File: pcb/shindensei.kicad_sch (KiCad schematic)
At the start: 0 parts

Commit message: Switch matrix output
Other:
- added sheet Channel Switch Matrix (switch_matrix.kicad_sch)
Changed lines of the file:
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@@
     (comment 1 "${Project}")
+  )
+  (sheet (at 143.51 88.9) (size 33.02 29.21) (fields_autoplaced)
+    (stroke (width 0.1524) (type solid))
+    (fill (color 0 0 0 0.0000))
+    (property "Sheetname" "Channel Switch Matrix" (at 143.51 88.1884 0)
+      (effects (font (size 1.27 1.27)) (justify left bottom))
+    )
+    (property "Sheetfile" "switch_matrix.kicad_sch" (at 143.51 118.6946 0)
+      (effects (font (size 1.27 1.27)) (justify left top))
+    )
+    (pin "CH1_B" output (at 176.53 96.52 0)
+      (effects (font (size 1.27 1.27)) (justify right))
+    )
+    (pin "PLS_A" input (at 163.83 88.9 90)
+      (effects (font (size 1.27 1.27)) (justify right))
+    )
+    (pin "PLS_B" input (at 154.94 88.9 90)
+      (effects (font (size 1.27 1.27)) (justify right))
+    )
+    (pin "CH1_A" output (at 176.53 93.98 0)
+      (effects (font (size 1.27 1.27)) (justify right))
+    )
+    (pin "CH2_B" output (at 176.53 111.76 0)
+      (effects (font (size 1.27 1.27)) (justify right))
+    )
+    (pin "CH2_A" output (at 176.53 109.22 0)
+      (effects (font (size 1.27 1.27)) (justify right))
+    )
+    (pin "OUT_A0" input (at 143.51 100.33 180)
+      (effects (font (size 1.27 1.27)) (justify left))
+    )
+    (pin "OUT_A1" input (at 143.51 106.68 180)
+      (effects (font (size 1.27 1.27)) (justify left))
+    )
+    (instances
+      (project "shindensei"
+        (path "/958b377d-2cd7-45e0-91dd-b2d6e2ab8826" (page "2"))
+      )
+    )
   )
   (sheet_instances

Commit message: Pulse control WiP
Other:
- added sheet Pulse Control (pulse_control.kicad_sch)
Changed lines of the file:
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@@
     (comment 1 "${Project}")
+  )
+  (sheet (at 120.65 45.72) (size 26.67 21.59) (fields_autoplaced)
+    (stroke (width 0.1524) (type solid))
+    (fill (color 0 0 0 0.0000))
+    (property "Sheetname" "Pulse Control" (at 120.65 45.0084 0)
+      (effects (font (size 1.27 1.27)) (justify left bottom))
+    )
+    (property "Sheetfile" "pulse_control.kicad_sch" (at 120.65 67.8946 0)
+      (effects (font (size 1.27 1.27)) (justify left top))
+    )
+    (instances
+      (project "shindensei"
+        (path "/958b377d-2cd7-45e0-91dd-b2d6e2ab8826" (page "2"))
+      )
+    )
   )
   (sheet (at 143.51 88.9) (size 33.02 29.21) (fields_autoplaced)

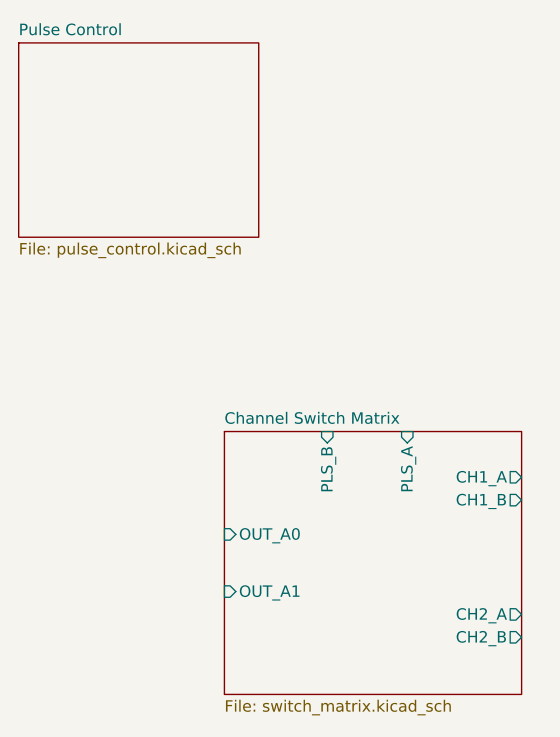
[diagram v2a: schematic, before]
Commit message: Added pulse control harmonized resistor values
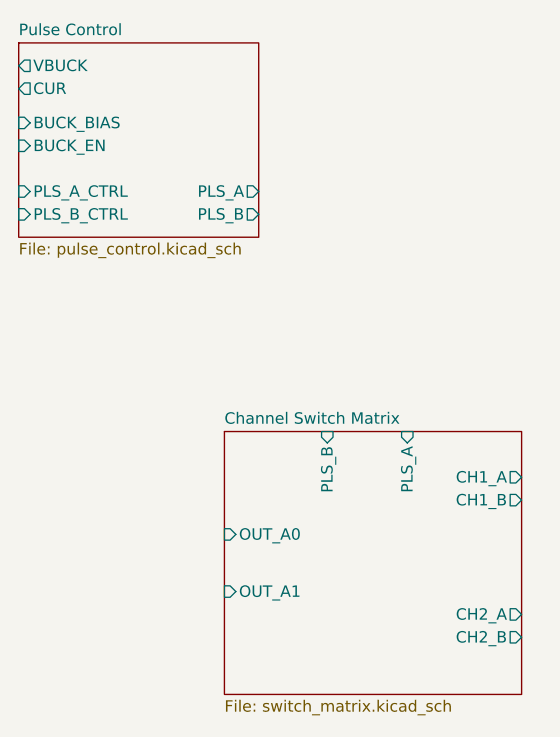
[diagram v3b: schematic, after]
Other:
- sheet Pulse Control ports: added BUCK_BIAS, BUCK_EN, CUR, PLS_A, PLS_A_CTRL, PLS_B, PLS_B_CTRL, VBUCK; removed none
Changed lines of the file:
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@@
       (effects (font (size 1.27 1.27)) (justify left top))
+    )
+    (pin "CUR" output (at 120.65 50.8 180)
+      (effects (font (size 1.27 1.27)) (justify left))
+    )
+    (pin "BUCK_BIAS" input (at 120.65 54.61 180)
+      (effects (font (size 1.27 1.27)) (justify left))
+    )
+    (pin "VBUCK" output (at 120.65 48.26 180)
+      (effects (font (size 1.27 1.27)) (justify left))
+    )
+    (pin "BUCK_EN" input (at 120.65 57.15 180)
+      (effects (font (size 1.27 1.27)) (justify left))
+    )
+    (pin "PLS_B" output (at 147.32 64.77 0)
+      (effects (font (size 1.27 1.27)) (justify right))
+    )
+    (pin "PLS_A" output (at 147.32 62.23 0)
+      (effects (font (size 1.27 1.27)) (justify right))
+    )
+    (pin "PLS_B_CTRL" input (at 120.65 64.77 180)
+      (effects (font (size 1.27 1.27)) (justify left))
+    )
+    (pin "PLS_A_CTRL" input (at 120.65 62.23 180)
+      (effects (font (size 1.27 1.27)) (justify left))
     )
     (instances
